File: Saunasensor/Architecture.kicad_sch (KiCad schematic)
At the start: 3 parts, among them U1 BME280, U2 AM2302, U5 DS18B20

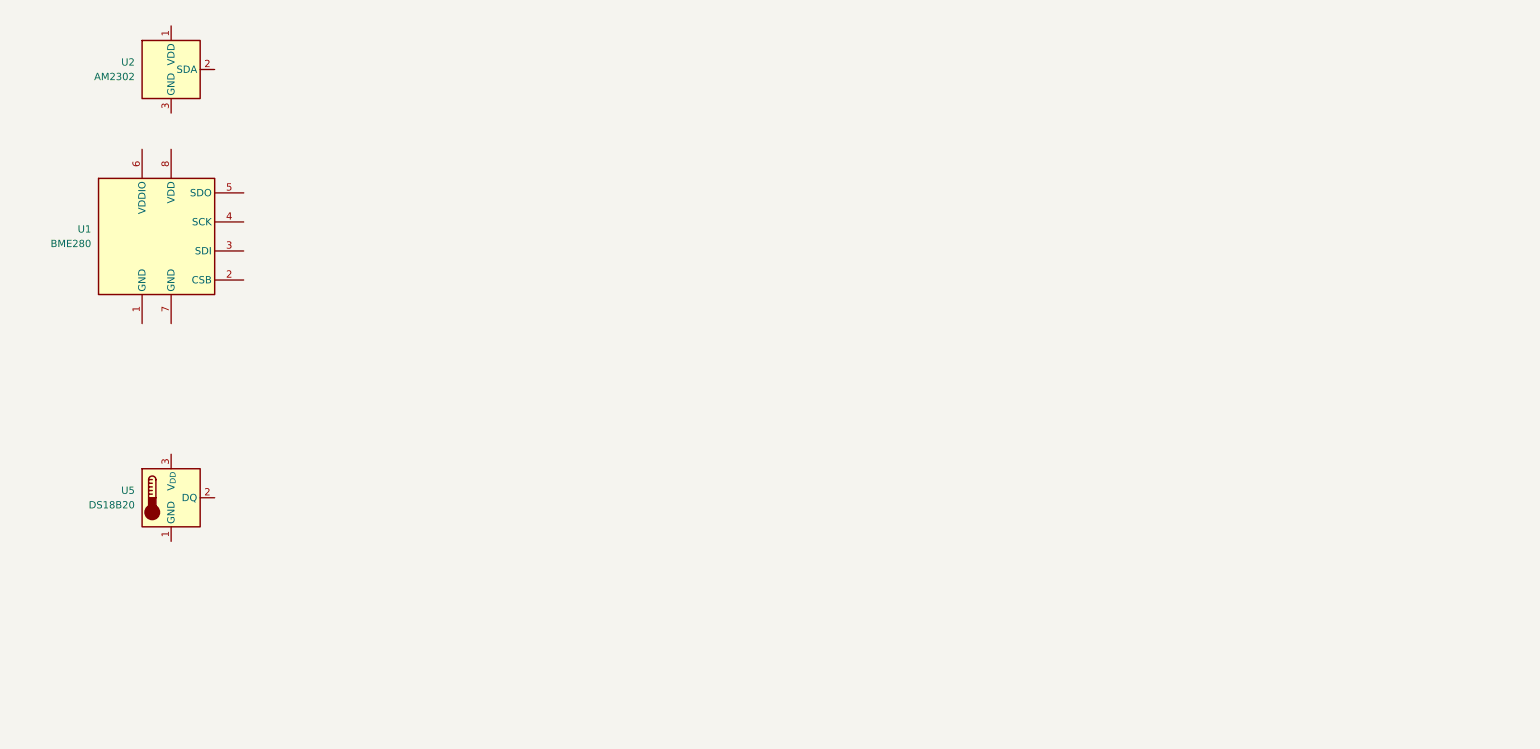
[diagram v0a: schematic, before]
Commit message: Schematic work
* added sensors
* added power supply
* added MCU
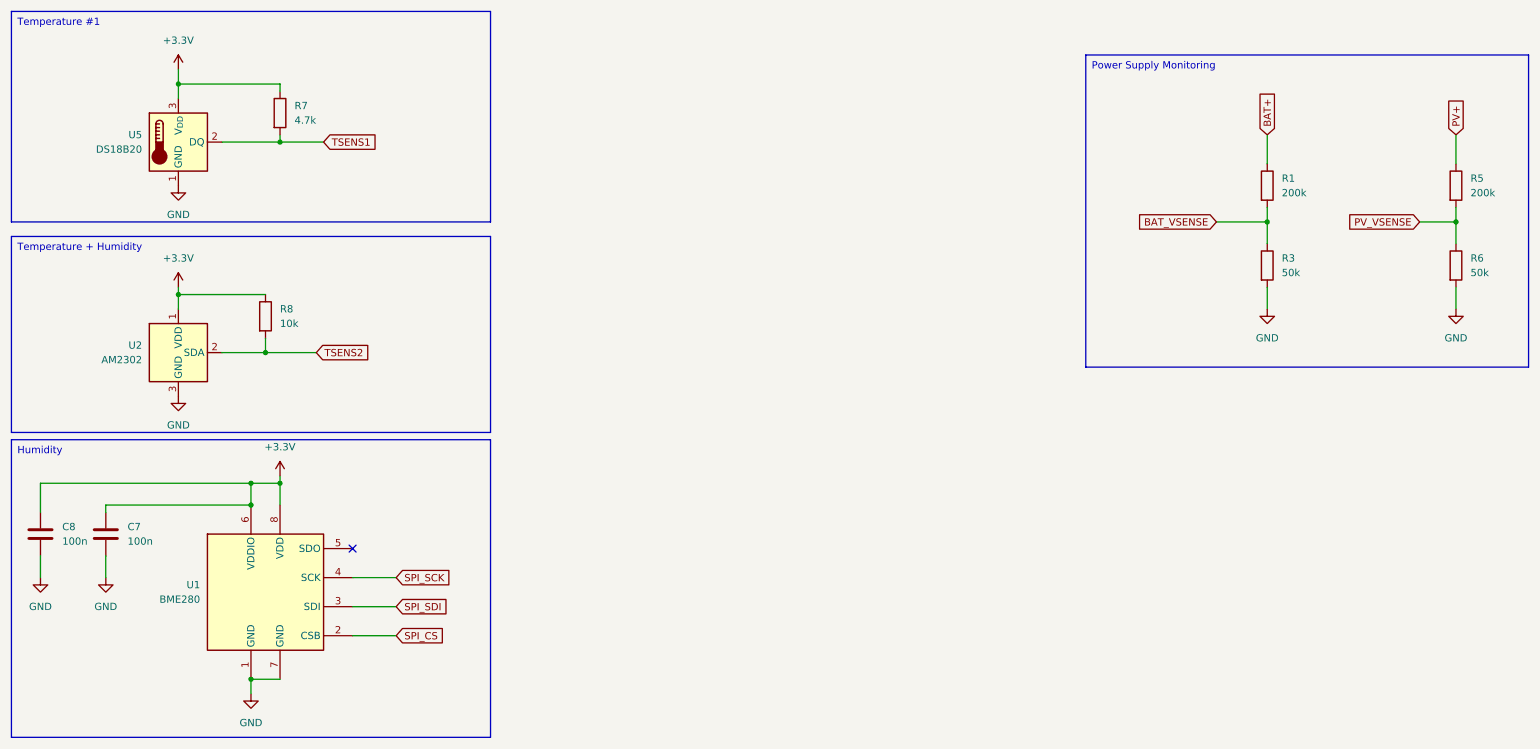
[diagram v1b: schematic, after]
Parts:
- added C7, C8: 100n, symbol Device:C
- added R1, R5: 200k, symbol Device:R
- added R3, R6: 50k, symbol Device:R
- added R7: 4.7k, symbol Device:R
- added R8: 10k, symbol Device:R
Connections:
- net GND: now reaches U1.1 (GND)
- net GND: now also U1.7 (GND), U2.3 (GND), U2.4 (GND), U5.1 (GND), C7.2, C8.2, R3.2, R6.2
- net SPI_CS: now reaches U1.2 (CSB)
- net SPI_SDI: now reaches U1.3 (SDI)
- net SPI_SCK: now reaches U1.4 (SCK)
- net +3.3V: now reaches U1.6 (VDDIO)
- net +3.3V: now also U1.8 (VDD), U2.1 (VDD), U5.3 (V_{DD}), C7.1, C8.1, R7.1, R8.1
- net TSENS1: now reaches U5.2 (DQ)
- net TSENS1: now also R7.2
- net TSENS2: now reaches U2.2 (SDA)
- net TSENS2: now also R8.2
- new net BAT+: R1.1
- new net BAT_VSENSE: R1.2, R3.1
- new net PV+: R5.1
- new net PV_VSENSE: R5.2, R6.1
- no-connect marks 0 -> 1
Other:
- moved on the sheet: U1, U2, U5

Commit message: Footprints
assigned footprints to components
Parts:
- C7, C8: footprint (none) -> Capacitor_SMD:C_0805_2012Metric
- R1, R3, R5, R6, R7, R8: footprint (none) -> Resistor_SMD:R_0805_2012Metric
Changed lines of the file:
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@@
 			)
 		)
-		(property "Footprint" ""
+		(property "Footprint" "Capacitor_SMD:C_0805_2012Metric"
 			(at 30.1752 109.22 0)
 			(effects
@@
 			)
 		)
-		(property "Footprint" ""
+		(property "Footprint" "Resistor_SMD:R_0805_2012Metric"
 			(at 55.372 67.31 90)
 			(effects
@@
 			)
 		)
-		(property "Footprint" ""
+		(property "Footprint" "Resistor_SMD:R_0805_2012Metric"
 			(at 263.652 58.42 90)
 			(effects
@@
 			)
 		)
-		(property "Footprint" ""
+		(property "Footprint" "Resistor_SMD:R_0805_2012Metric"
 			(at 263.652 44.45 90)
 			(effects
@@
 			)
 		)
-		(property "Footprint" ""
+		(property "Footprint" "Resistor_SMD:R_0805_2012Metric"
 			(at 230.632 44.45 90)
 			(effects
@@
 			)
 		)
-		(property "Footprint" ""
+		(property "Footprint" "Capacitor_SMD:C_0805_2012Metric"
 			(at 18.7452 109.22 0)
 			(effects
@@
 			)
 		)
-		(property "Footprint" ""
+		(property "Footprint" "Resistor_SMD:R_0805_2012Metric"
 			(at 230.632 58.42 90)
 			(effects
@@
 			)
 		)
-		(property "Footprint" ""
+		(property "Footprint" "Resistor_SMD:R_0805_2012Metric"
 			(at 57.912 31.75 90)
 			(effects
